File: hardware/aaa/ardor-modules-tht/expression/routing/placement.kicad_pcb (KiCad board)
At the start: 2 copper layers, 110 x 85 mm, 31 parts, among them J101 3V3 POWER INPUT + I2C TO HOST, J302 PASSIVE PEDAL INPUT / EXCITAT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, U301 Adafruit 1085 ADS1115 QT

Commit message: fix(hardware): use Hestore TVS diodes in hand-assembly modules
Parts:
- D301, D302: value SA5.0CA-E3/54 -> 1.5KE6.8CA; footprint Diode_THT:D_DO-15_P10.16mm_Horizontal -> Ardor_THT:D_TVS_DC_1.5KE_P15.24mm
- moved D301 2.54 mm to (54.9, 67.5)
- moved D302 2.54 mm to (54.9, 97.5)

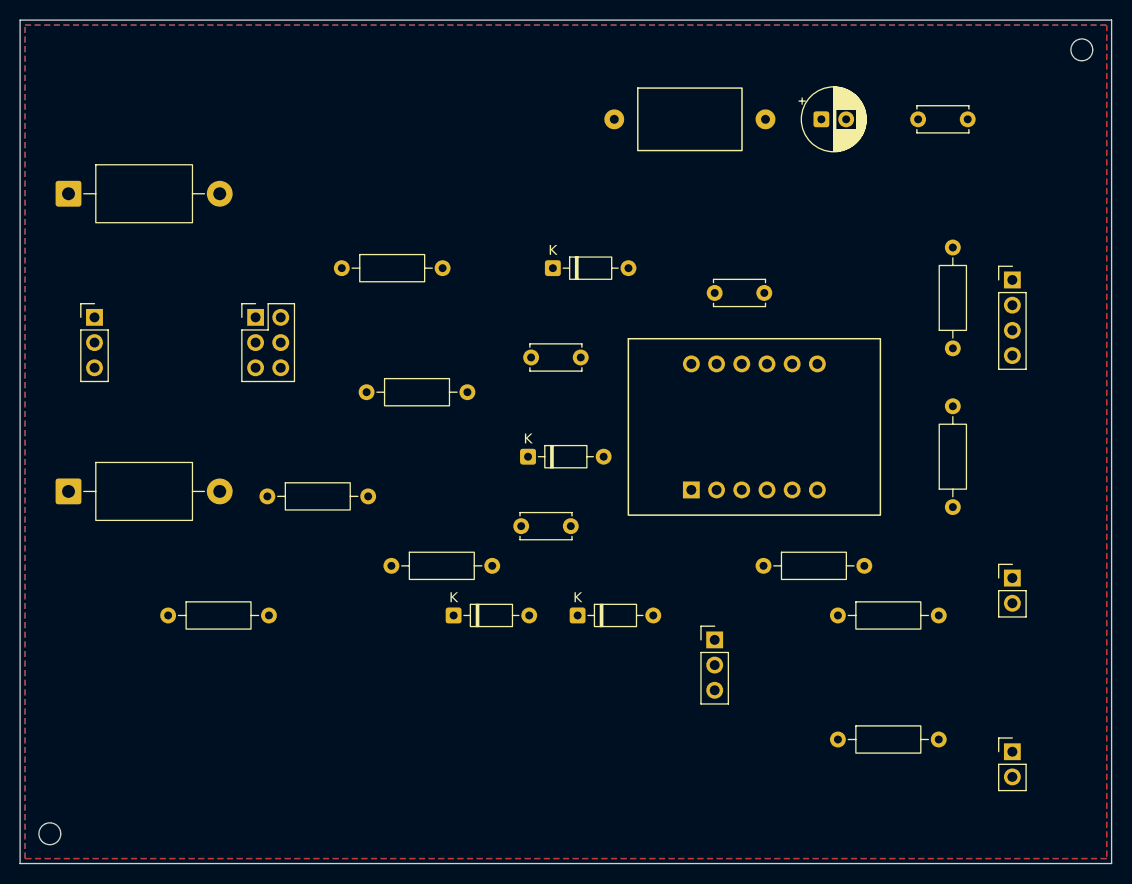
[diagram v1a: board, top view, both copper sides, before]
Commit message: feat(hardware): compact layouts and adopt Hestore module packages
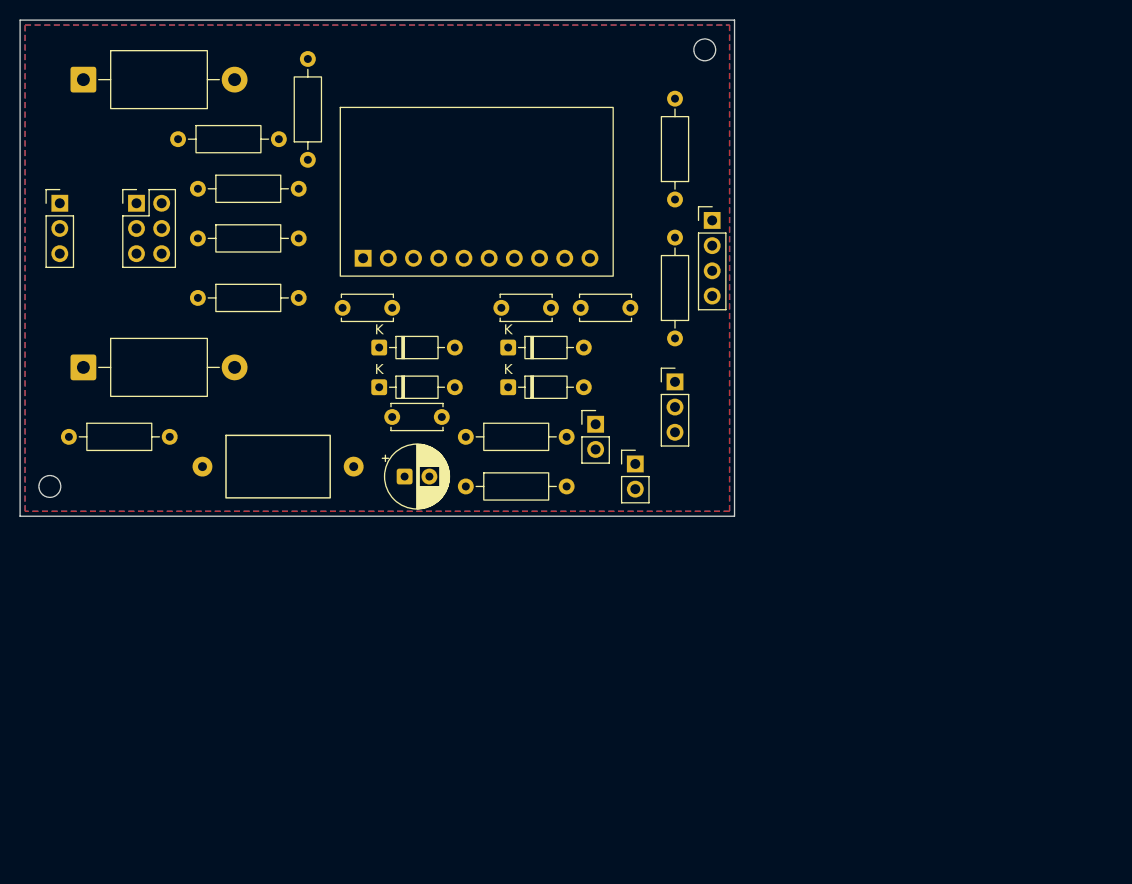
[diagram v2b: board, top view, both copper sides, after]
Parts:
- U301: value Adafruit 1085 ADS1115 QT -> ADS1115-M; footprint Ardor_THT:Adafruit_ADS1115_1085_STEMMA_QT -> Ardor_THT:ADS1115_M_HESTORE_10041798
- moved R307 73.0 mm to (65.9, 62.0)
- moved C102 60.9 mm to (87.5, 90.0)
- moved C101 55.3 mm to (88.8, 96.0)
- moved FB101 54.3 mm to (68.4, 95.0)
- moved JP304 47.8 mm to (112.0, 94.7)
- moved R309 45.3 mm to (94.9, 97.0)
- moved JP303 44.8 mm to (108.0, 90.7)
- moved R304 41.8 mm to (79.0, 64.1), turned to 90 degrees
- moved R308 41.6 mm to (94.9, 92.0)
- moved H2 38.0 mm to (119.0, 53.0)
- moved C303 37.5 mm to (82.5, 79.0)
- moved H1 35.0 mm to (53.0, 97.0)
- moved R306 32.8 mm to (116.0, 82.1)
- moved U301 32.8 mm to (96.0, 74.0)
- moved R305 31.8 mm to (116.0, 68.1)
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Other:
- board size 110 x 85 mm -> 72 x 50 mm
